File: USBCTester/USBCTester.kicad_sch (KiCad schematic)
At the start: 92 parts, among them J1 USB4080-03-A, J2 USB4080-03-A, J3 Conn_01x14, J4 Conn_01x03, J6 Conn_01x03, SW1 SW_Push, U1 74HC595, U2 74HC595, U3 74HC595, U4 74HC595, U5 74HC595, U6 74HC595, U7 RaspberryPi_Pico

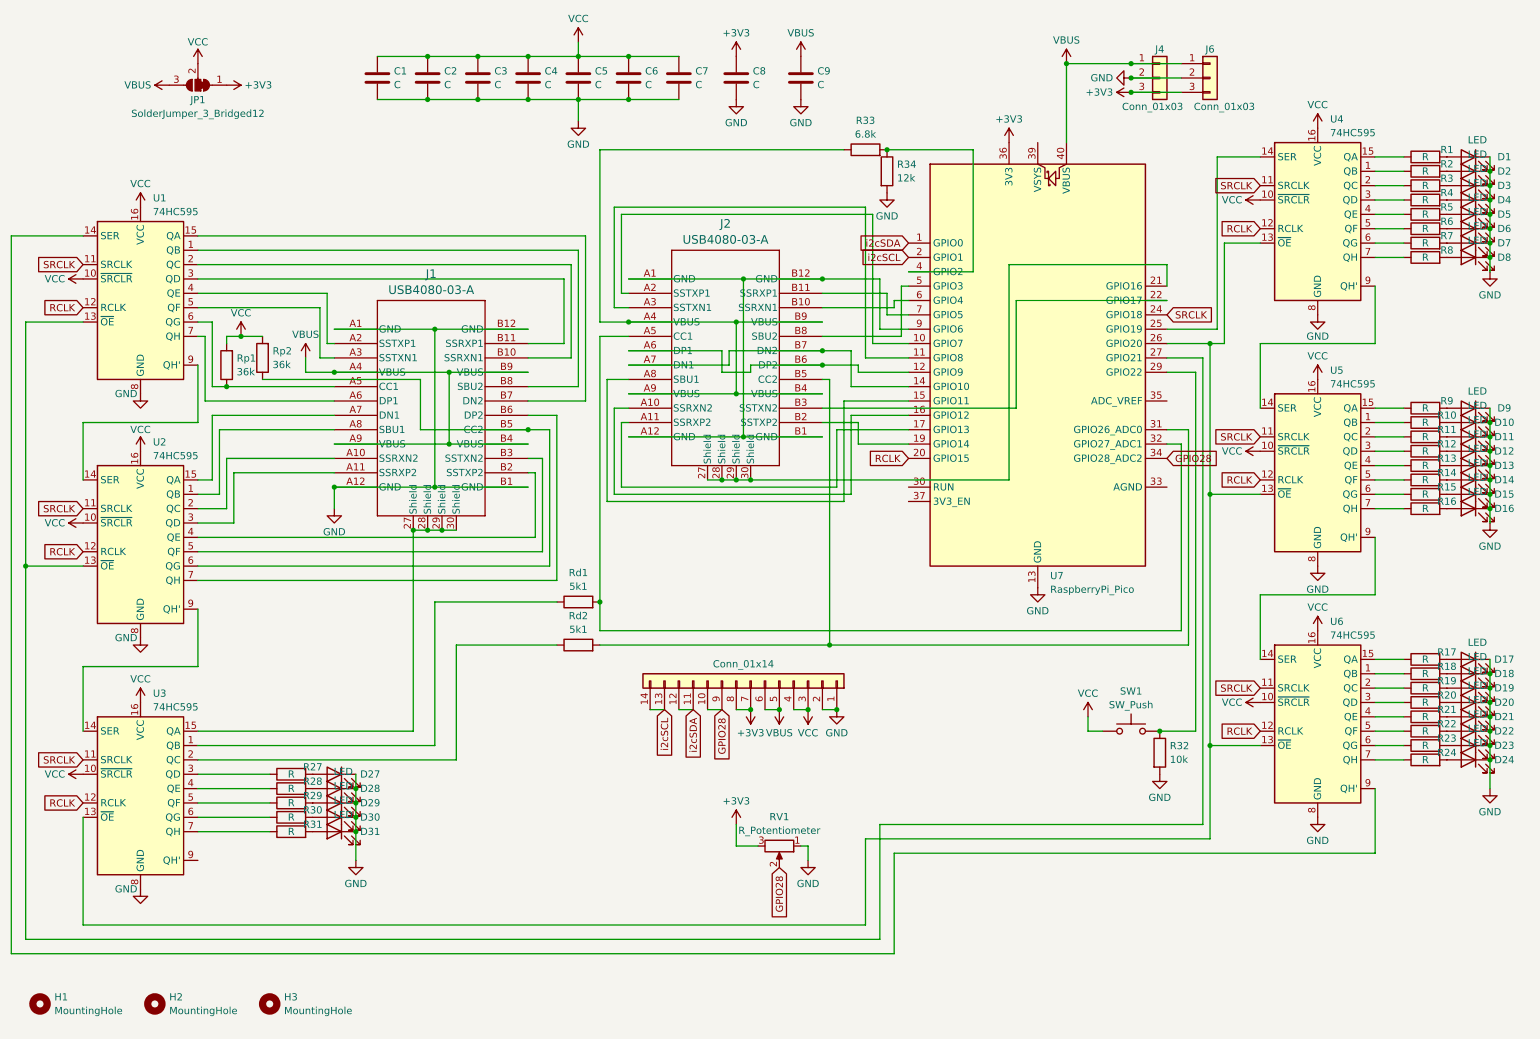
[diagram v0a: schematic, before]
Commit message: revision 1.2, add another shift register and fix the production files
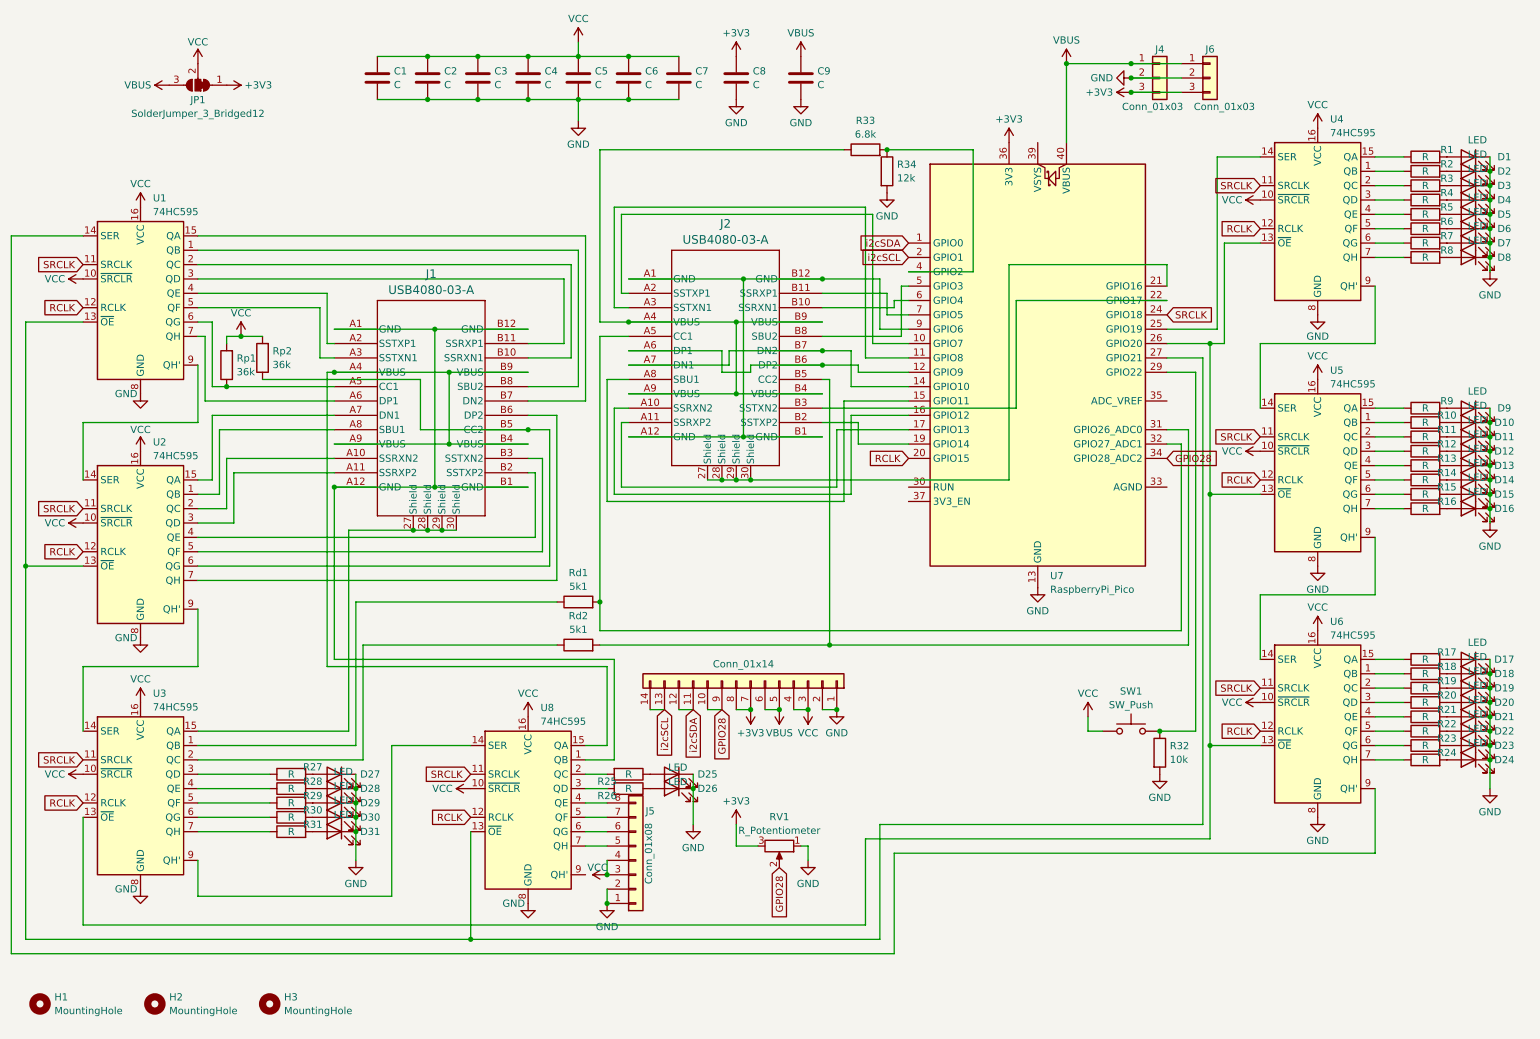
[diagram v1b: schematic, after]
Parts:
- added D25, D26: LED, LED_SMD:LED_0603_1608Metric, symbol Device:LED
- added J5: Conn_01x08, Connector_PinHeader_2.54mm:PinHeader_2x04_P2.54mm_Vertical, symbol Connector_Generic:Conn_01x08
- added R25, R26: R, Resistor_SMD:R_0603_1608Metric, symbol Device:R
- added U8: 74HC595, Package_SO:SOIC-16_3.9x9.9mm_P1.27mm, symbol 74xx:74HC595
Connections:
- net GND: now also D25.1 (K), D26.1 (K), J5.1 (Pin_1), J5.2 (Pin_2), U8.8 (GND); no longer J1.A1 (GND), J1.A12 (GND), J1.B1 (GND), J1.B12 (GND)
- net RCLK: now also U8.12 (RCLK)
- net SRCLK: now also U8.11 (SRCLK)
- net VBUS: no longer J1.A4 (VBUS), J1.A9 (VBUS), J1.B4 (VBUS), J1.B9 (VBUS)
- net VCC: now also J5.3 (Pin_3), J5.4 (Pin_4), U8.10 (~{SRCLR}), U8.16 (VCC)
- net at U1.13 (~{OE}), U2.13 (~{OE}), U7.27 (GPIO21): now also U8.13 (~{OE})
- net at U3.9 (QH'): now also U8.14 (SER)
- new net: D25.2 (A), R25.1
- new net: J1.A1 (GND), J1.A12 (GND), J1.B1 (GND), J1.B12 (GND), U8.1 (QB)
- new net: J1.A4 (VBUS), J1.A9 (VBUS), J1.B4 (VBUS), J1.B9 (VBUS), U8.15 (QA)
- new net: D26.2 (A), R26.1
- new net: R26.2, U8.3 (QD)
- new net: J5.5 (Pin_5), U8.7 (QH)
- new net: J5.6 (Pin_6), U8.6 (QG)
- new net: J5.7 (Pin_7), U8.5 (QF)
- new net: J5.8 (Pin_8), U8.4 (QE)
- new net: R25.2, U8.2 (QC)

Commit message: update PCB and Schematic files
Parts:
- R34: value 12k -> 18k
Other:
- note added: "1 1"
- note added: "1.1"
- note added: "Author:"
- note added: "Patrick Leiser"
- note added: "Spring 2024"
- note added: "USB C Tester"
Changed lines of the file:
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@@
+		)
+	)
+	(text "Author:"
+		(exclude_from_sim no)
+		(at 257.048 189.738 0)
+		(effects
+			(font
+				(size 1.5 1.5)
+				(color 132 0 0 1)
+			)
+		)
+	)
+	(text "Spring 2024"
+		(exclude_from_sim no)
+		(at 213.36 193.294 0)
+		(effects
+			(font
+				(size 1.27 1.27)
+			)
+		)
+	)
+	(text "Patrick Leiser"
+		(exclude_from_sim no)
+		(at 273.05 189.738 0)
+		(effects
+			(font
+				(size 2 2)
+			)
+		)
+	)
+	(text "1.1"
+		(exclude_from_sim no)
+		(at 270.002 193.294 0)
+		(effects
+			(font
+				(size 1.5 1.5)
+			)
+		)
+	)
+	(text "1  1"
+		(exclude_from_sim no)
+		(at 187.198 183.388 0)
+		(effects
+			(font
+				(size 1.27 1.27)
+			)
+		)
+	)
+	(text "USB C Tester"
+		(exclude_from_sim no)
+		(at 196.596 189.738 0)
+		(effects
+			(font
+				(size 2 2)
+				(thickness 0.4)
+				(bold yes)
+			)
 		)
 	)
@@
 		(fields_autoplaced yes)
 		(property "Reference" "R34"
-			(at 174.498 41.9679 0)
+			(at 174.498 41.9678 0)
 			(effects
 				(font
@@
 			)
 		)
-		(property "Value" "12k"
+		(property "Value" "18k"
 			(at 174.498 44.3921 0)
 			(effects
